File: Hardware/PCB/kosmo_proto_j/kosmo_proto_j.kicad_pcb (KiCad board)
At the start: 2 copper layers, 100 x 55 mm, 567 parts, among them J1 Synth_power_2x5, J10 1x1, J100 1x1, J101 1x1, J102 1x1, J103 1x1, J104 1x1, J105 1x1, J106 1x1, J107 1x1, J108 1x1, J109 1x1, J11 1x1, J110 1x1, J111 1x1, J112 1x1, J113 1x1, J114 1x1, J115 1x1, J116 1x1, J117 1x1, J118 1x1, J119 1x1, J12 1x1, J120 1x1, J121 1x1, J122 1x1, J123 1x1, J124 1x1, J125 1x1, J126 1x1, J127 1x1, J128 1x1, J129 1x1, J13 1x1, J130 1x1, J131 1x1, J132 1x1, J133 1x1, J134 1x1, J135 1x1, J136 1x1, J137 1x1, J138 1x1, J139 1x1, J14 1x1, J140 1x1, J141 1x1, J142 1x1, J143 1x1, J144 1x1, J145 1x1, J146 1x1, J147 1x1, J148 1x1, J149 1x1, J15 1x1, J150 1x1, J151 1x1, J152 1x1, J153 1x1, J154 1x1, J155 1x1, J156 1x1, J157 1x1, J158 1x1, J159 1x1, J16 1x1, J160 1x1, J161 1x1, J162 1x1, J163 1x1, J164 1x1, J165 1x1, J166 1x1, J167 1x1, J168 1x1, J169 1x1, J17 1x1, J170 1x1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

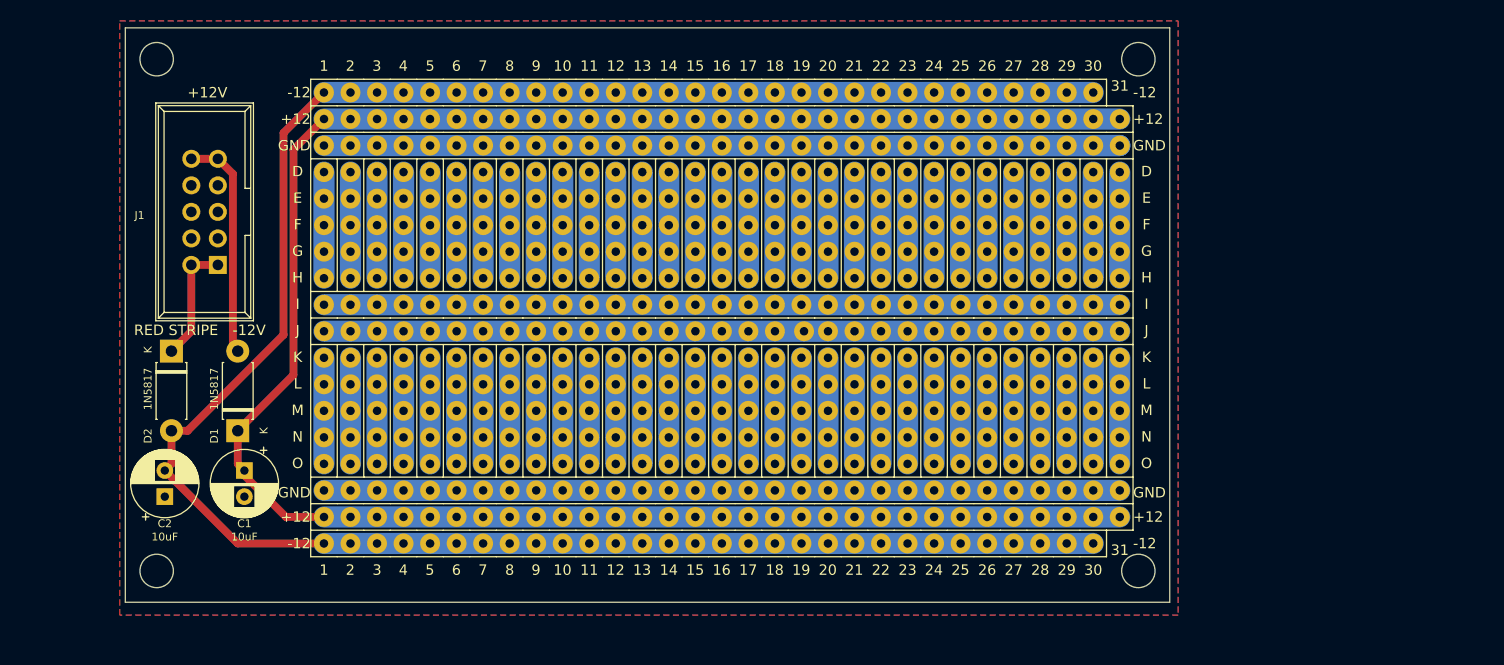
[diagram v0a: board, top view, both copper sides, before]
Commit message: Narrower version with jacks (kosmo_proto_j)
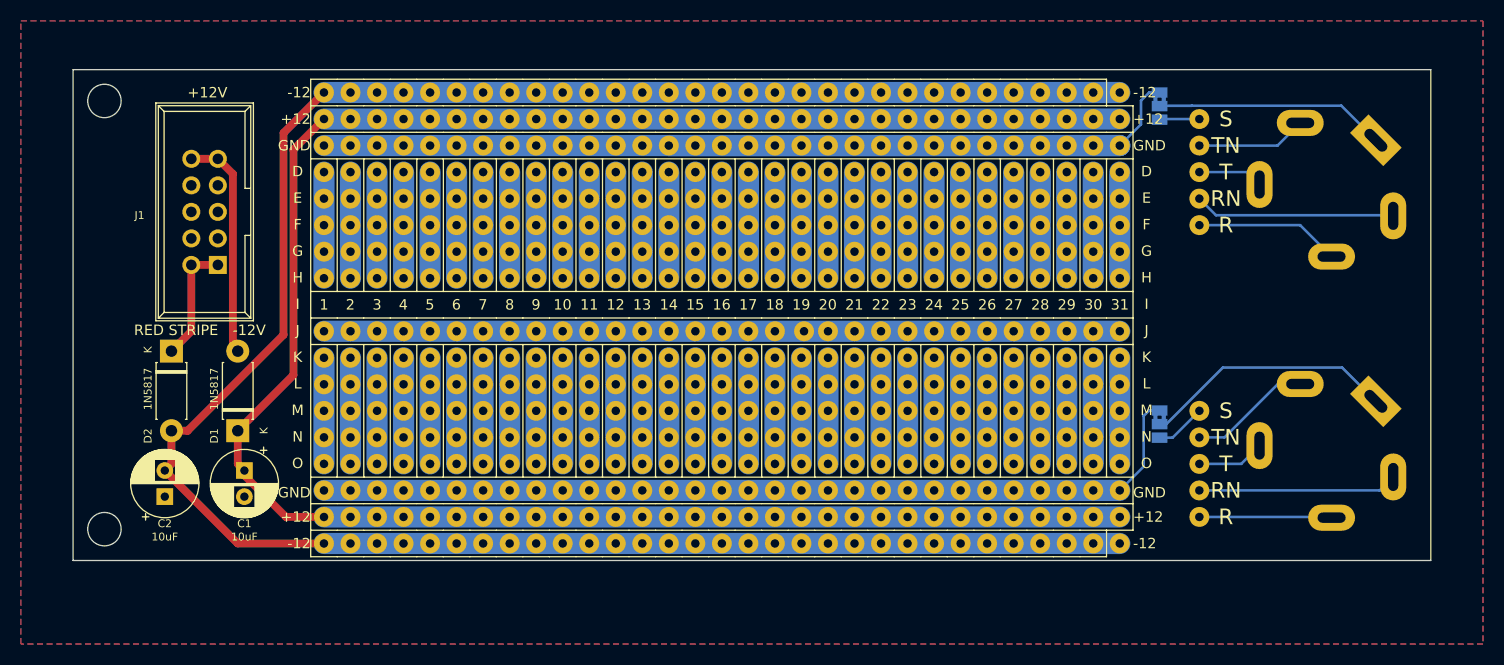
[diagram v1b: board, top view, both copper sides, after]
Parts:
- removed the H2 at (142.8, 105.5)
- removed H4: MountingHole, ao_tht:MountingHole_3.2mm_M3
- removed the J10 at (64.8, 80.0)
- removed the J100 at (90.2, 80.0)
- removed the J109 at (92.7, 80.0)
- removed the J118 at (95.2, 80.0)
- removed the J127 at (97.8, 80.0)
- removed the J136 at (100.3, 80.0)
- removed the J145 at (102.9, 80.0)
- removed the J154 at (105.4, 80.0)
- removed the J163 at (108.0, 80.0)
- removed the J172 at (110.5, 80.0)
- removed the J181 at (113.0, 80.0)
- removed the J19 at (67.3, 80.0)
- removed the J190 at (115.6, 80.0)
- removed the J199 at (118.1, 80.0)
- removed the J208 at (120.7, 80.0)
- removed the J217 at (123.2, 80.0)
- removed the J226 at (125.7, 80.0)
- removed the J235 at (128.3, 80.0)
- removed the J262 at (135.9, 80.0)
- removed the J271 at (138.4, 80.0)
- removed the J28 at (69.8, 80.0)
- removed the J280 at (141.0, 80.0)
- removed the J37 at (72.4, 80.0)
- removed the J46 at (74.9, 80.0)
- removed the J55 at (77.5, 80.0)
- removed the J64 at (80.0, 80.0)
- removed the J73 at (82.5, 80.0)
- removed the J82 at (85.1, 80.0)
- removed the J91 at (87.6, 80.0)
- added J2: AudioJack3_SwitchTR, ao_tht:Jack_6.35mm_PJ_629HAN_slots, B.Cu at (160.8, 69.0)
- added J252: 1x1, ao_tht:Perf_Board_Hole, F.Cu at (148.6, 72.4)
- added J254: 1x1, ao_tht:Perf_Board_Hole, F.Cu at (148.6, 100.3)
- added J255: 1x1, ao_tht:Perf_Board_Hole, F.Cu at (148.6, 95.2)
- added J256: 1x1, ao_tht:Perf_Board_Hole, F.Cu at (148.6, 69.8)
- added J257: 1x1, ao_tht:Perf_Board_Hole, F.Cu at (148.6, 64.8)
- added J258: 1x1, ao_tht:Perf_Board_Hole, F.Cu at (148.6, 97.8)
- added J259: 1x1, ao_tht:Perf_Board_Hole, F.Cu at (148.6, 92.7)
- added J260: 1x1, ao_tht:Perf_Board_Hole, F.Cu at (148.6, 62.2)
- added J261: 1x1, ao_tht:Perf_Board_Hole, F.Cu at (148.6, 90.2)
- added J3: AudioJack3_SwitchTR, ao_tht:Jack_6.35mm_PJ_629HAN_slots, B.Cu at (160.8, 94.0)
- added J540: 1x1, ao_tht:Perf_Board_Hole, F.Cu at (141.0, 102.9)
- added JP1: SolderJumper_3_Bridged12, Jumper:SolderJumper-3_P1.3mm_Bridged2Bar12_Pad1.0x1.5mm, B.Cu at (144.8, 61.0)
- added JP2: SolderJumper_3_Bridged12, Jumper:SolderJumper-3_P1.3mm_Bridged2Bar12_Pad1.0x1.5mm, B.Cu at (144.8, 91.4)
- moved GRAF1 94.1 mm to (148.6, 82.0), turned to 270 degrees
- moved GRAF2 31.1 mm to (60.3, 91.1), turned to 270 degrees
- moved J244 22.7 mm to (141.0, 59.7)
- moved J253 19.8 mm to (148.6, 67.3)
- moved H1 6.40 mm to (43.8, 101.5)
- moved H2 6.40 mm to (43.8, 60.5)
- renumbered H3 to H2, J8 to J10, J110 to J100, J111 to J101, J112 to J102, J113 to J103, J114 to J104, J115 to J105, J116 to J106, J117 to J107, J119 to J108, J120 to J109, J9 to J11, J121 to J110, J122 to J111, J123 to J112, J124 to J113, J125 to J114, J126 to J115, J128 to J116, J129 to J117, J130 to J118, J131 to J119, J11 to J12, J132 to J120, J133 to J121, J134 to J122, J135 to J123, J137 to J124, J138 to J125, J139 to J126, J140 to J127, J141 to J128, J142 to J129, J12 to J13, J143 to J130, J144 to J131, J146 to J132, J147 to J133, J148 to J134, J149 to J135, J150 to J136, J151 to J137, J152 to J138, J153 to J139, J13 to J14, J155 to J140, J156 to J141, J157 to J142, J158 to J143, J159 to J144, J160 to J145, J161 to J146, J162 to J147, J164 to J148, J165 to J149, J14 to J15, J166 to J150, J167 to J151, J168 to J152, J169 to J153, J170 to J154, J171 to J155, J173 to J156, J174 to J157, J175 to J158, J176 to J159, J15 to J16, J177 to J160, J178 to J161, J179 to J162, J180 to J163, J182 to J164, J183 to J165, J184 to J166, J185 to J167, J186 to J168, J187 to J169, J16 to J17, J188 to J170, J189 to J171, J191 to J172, J192 to J173, J193 to J174, J194 to J175, J195 to J176, J196 to J177, J197 to J178, J198 to J179, J17 to J18, J200 to J180, J201 to J181, J202 to J182, J203 to J183, J204 to J184, J205 to J185, J206 to J186, J207 to J187, J209 to J188, J210 to J189, J18 to J19, J211 to J190, J212 to J191, J213 to J192, J214 to J193, J215 to J194, J216 to J195, J218 to J196, J219 to J197, J220 to J198, J221 to J199, J222 to J200, J223 to J201, J224 to J202, J225 to J203, J227 to J204, J228 to J205, J229 to J206, J230 to J207, J231 to J208, J232 to J209, J233 to J210, J234 to J211, J236 to J212, J237 to J213, J238 to J214, J239 to J215, J240 to J216, J241 to J217, J242 to J218, J243 to J219, J245 to J220, J246 to J221, J247 to J222, J248 to J223, J249 to J224, J250 to J225, J251 to J226, J252 to J227, J254 to J228, J255 to J229, J256 to J230, J257 to J231, J258 to J232, J259 to J233, J260 to J234, J261 to J235, J263 to J236, J264 to J237, J265 to J238, J266 to J239, J267 to J240, J268 to J241, J269 to J242, J270 to J243, J273 to J245, J274 to J246, J275 to J247, J276 to J248, J277 to J249, J278 to J250, J279 to J251, J281 to J262, J282 to J263, J283 to J264, J284 to J265, J285 to J266, J286 to J267, J287 to J268, J288 to J269, J289 to J270, J290 to J271, J291 to J272, J292 to J273, J293 to J274, J294 to J275, J295 to J276, J296 to J277, J297 to J278, J298 to J279, J29 to J28, J299 to J280, J300 to J281, J301 to J282, J302 to J283, J303 to J284, J304 to J285, J305 to J286, J306 to J287, J307 to J288, J308 to J289, J30 to J29, J309 to J290, J310 to J291, J311 to J292, J312 to J293, J313 to J294, J314 to J295, J315 to J296, J316 to J297, J317 to J298, J318 to J299, J31 to J30, J319 to J300, J320 to J301, J321 to J302, J322 to J303, J323 to J304, J324 to J305, J325 to J306, J326 to J307, J327 to J308, J328 to J309, J32 to J31, J329 to J310, J330 to J311, J331 to J312, J332 to J313, J333 to J314, J334 to J315, J335 to J316, J336 to J317, J337 to J318, J338 to J319, J33 to J32, J339 to J320, J340 to J321, J341 to J322, J342 to J323, J343 to J324, J344 to J325, J345 to J326, J346 to J327, J347 to J328, J348 to J329, J34 to J33, J349 to J330, J350 to J331, J351 to J332, J352 to J333, J353 to J334, J354 to J335, J355 to J336, J356 to J337, J357 to J338, J358 to J339, J35 to J34, J359 to J340, J360 to J341, J361 to J342, J362 to J343, J363 to J344, J364 to J345, J365 to J346, J366 to J347, J367 to J348, J368 to J349, J36 to J35, J369 to J350, J370 to J351, J371 to J352, J372 to J353, J373 to J354, J374 to J355, J375 to J356, J376 to J357, J377 to J358, J378 to J359, J38 to J36, J379 to J360, J380 to J361, J381 to J362, J382 to J363, J383 to J364, J384 to J365, J385 to J366, J386 to J367, J387 to J368, J388 to J369, J39 to J37, J389 to J370, J390 to J371, J391 to J372, J392 to J373, J393 to J374, J394 to J375, J395 to J376, J396 to J377, J397 to J378, J398 to J379, J40 to J38, J399 to J380, J400 to J381, J401 to J382, J402 to J383, J403 to J384, J404 to J385, J405 to J386, J406 to J387, J407 to J388, J408 to J389, J41 to J39, J409 to J390, J410 to J391, J411 to J392, J412 to J393, J413 to J394, J414 to J395, J415 to J396, J416 to J397, J417 to J398, J418 to J399, J2 to J4, J42 to J40, J419 to J400, J420 to J401, J421 to J402, J422 to J403, J423 to J404, J424 to J405, J425 to J406, J426 to J407, J427 to J408, J428 to J409, J43 to J41, J429 to J410, J430 to J411, J431 to J412, J432 to J413, J433 to J414, J434 to J415, J435 to J416, J436 to J417, J437 to J418, J438 to J419, J44 to J42, J439 to J420, J440 to J421, J441 to J422, J442 to J423, J443 to J424, J444 to J425, J445 to J426, J446 to J427, J447 to J428, J448 to J429, J45 to J43, J449 to J430, J450 to J431, J451 to J432, J452 to J433, J453 to J434, J454 to J435, J455 to J436, J456 to J437, J457 to J438, J458 to J439, J47 to J44, J459 to J440, J460 to J441, J461 to J442, J462 to J443, J463 to J444, J464 to J445, J465 to J446, J466 to J447, J467 to J448, J468 to J449, J48 to J45, J469 to J450, J470 to J451, J471 to J452, J472 to J453, J473 to J454, J474 to J455, J475 to J456, J476 to J457, J477 to J458, J478 to J459, J49 to J46, J479 to J460, J480 to J461, J481 to J462, J482 to J463, J483 to J464, J484 to J465, J485 to J466, J486 to J467, J487 to J468, J488 to J469, J50 to J47, J489 to J470, J490 to J471, J491 to J472, J492 to J473, J493 to J474, J494 to J475, J495 to J476, J496 to J477, J497 to J478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
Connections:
- J244 pad 1: Net-(J10-Pad1) (its old number) -> -12V
- J253 pad 1: Net-(J10-Pad1) (its old number) -> Net-(J2-PadT)
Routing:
- net Net-(J10-Pad1) (its old number): track 76.2 -> 0.00 mm
- net Net-(J3-PadS): track 0.00 -> 24.3 mm
- net Net-(J2-PadS): track 0.00 -> 22.1 mm
- net Net-(J2-PadRN): track 0.00 -> 19.2 mm
- net Net-(J258-Pad1): track 0.00 -> 19.1 mm
- net GND: track 195.6 -> 212.6 mm
- net Net-(J2-PadR): track 0.00 -> 13.9 mm
- net Net-(J254-Pad1): track 0.00 -> 12.7 mm
- net Net-(J259-Pad1): track 0.00 -> 11.8 mm
- net Net-(J2-PadTN): track 0.00 -> 10.6 mm
- net Net-(J255-Pad1): track 0.00 -> 6.48 mm
- net Net-(J2-PadT): track 0.00 -> 6.25 mm
- net -12V: track 208.9 -> 214.0 mm
- net Net-(J261-Pad1): track 0.00 -> 4.87 mm
- net Net-(J260-Pad1): track 0.00 -> 3.81 mm
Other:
- board size 100 x 55 mm -> 130 x 47 mm
- board text added: "R"
- board text added: "RN"
- board text added: "S"
- board text added: "T"
- board text added: "TN"

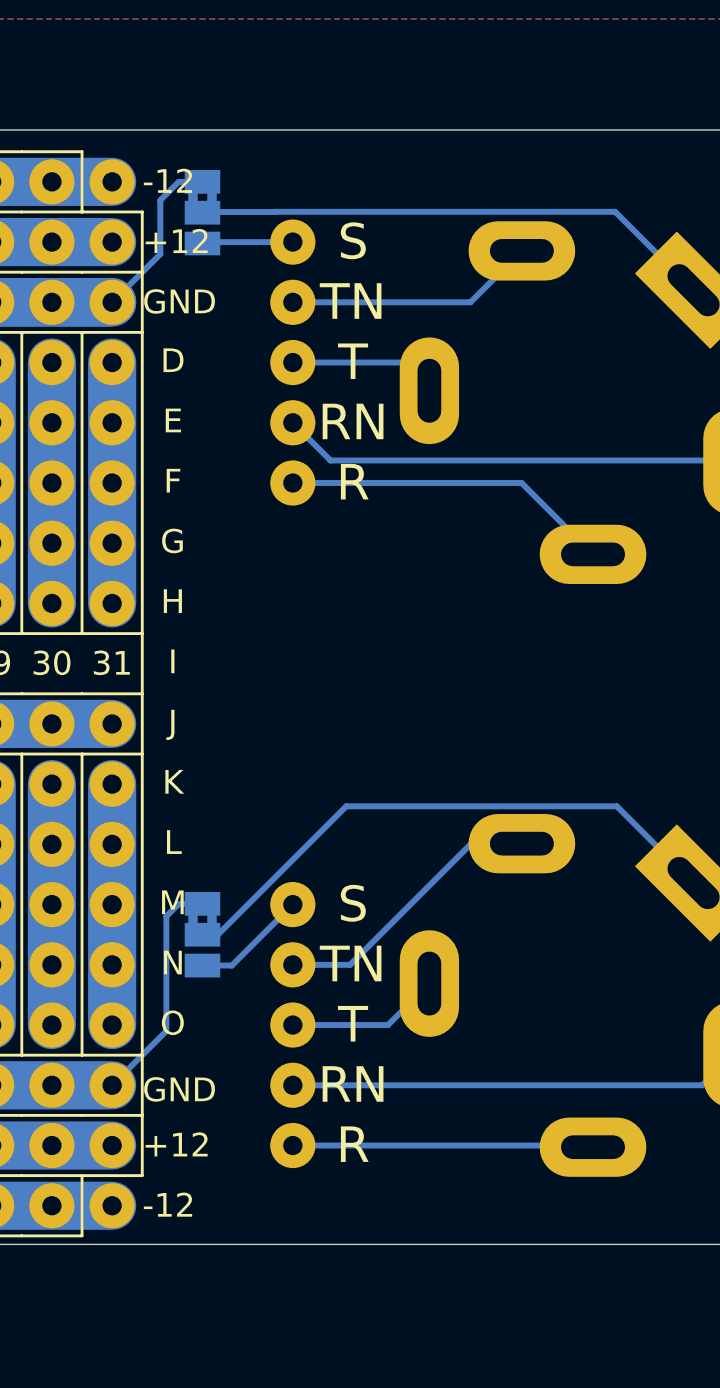
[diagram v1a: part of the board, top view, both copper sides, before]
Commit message: Jack labels; images
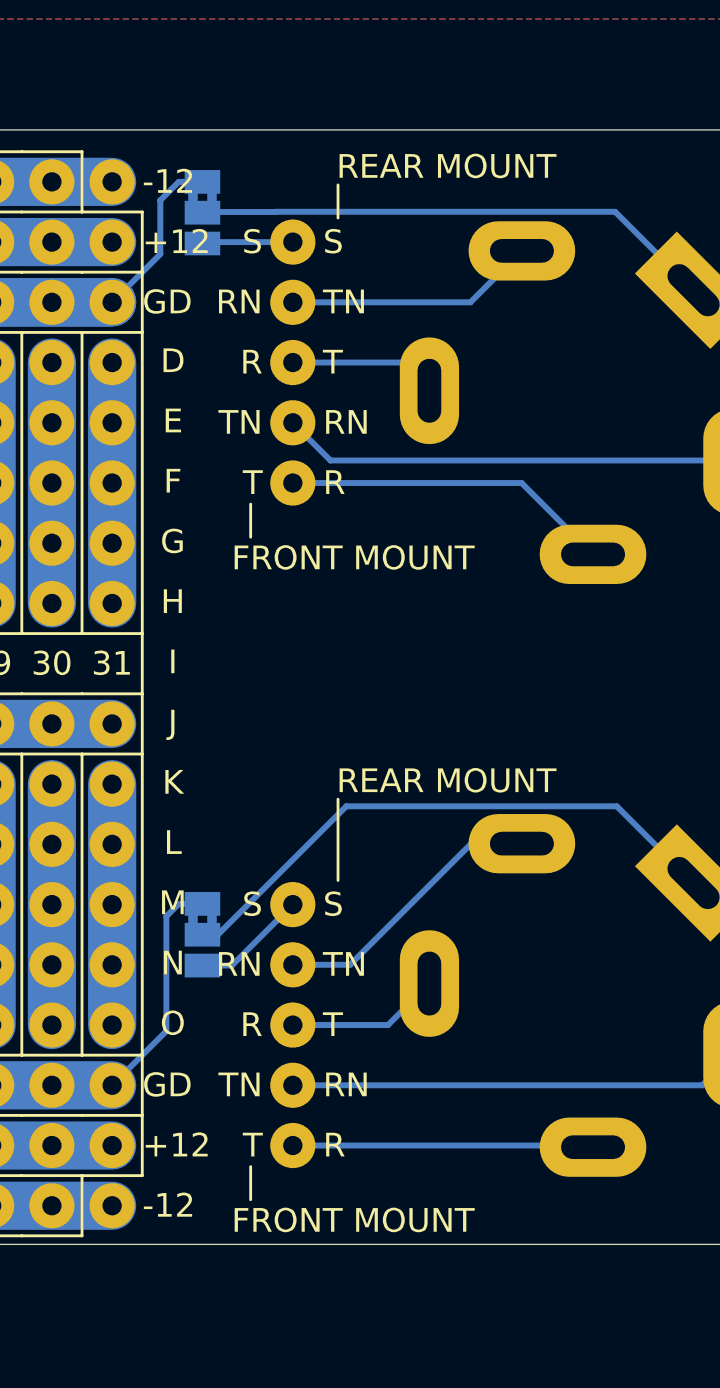
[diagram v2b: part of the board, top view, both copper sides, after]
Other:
- board text added: "FRONT MOUNT"
- board text added: "GD"
- board text added: "REAR MOUNT"

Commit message: more jacks mod, tweak original
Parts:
- D1, D2: footprint ao_tht:D_DO-41_SOD81_P7.62mm_Horizontal -> ao_tht:D_DO-41_SOD81_P10.16mm_Horizontal
- moved J1 2.54 mm to (54.6, 73.7)
- moved D2 2.01 mm to (49.5, 82.5)
- moved J2 2.00 mm to (162.8, 69.0)
- moved J252 2.00 mm to (150.6, 72.4)
- moved J253 2.00 mm to (150.6, 67.3)
- moved J254 2.00 mm to (150.6, 100.3)
- moved J255 2.00 mm to (150.6, 95.2)
- moved J256 2.00 mm to (150.6, 69.8)
- moved J257 2.00 mm to (150.6, 64.8)
- moved J258 2.00 mm to (150.6, 97.8)
- moved J259 2.00 mm to (150.6, 92.7)
- moved J260 2.00 mm to (150.6, 62.2)
- moved J261 2.00 mm to (150.6, 90.2)
- moved J3 2.00 mm to (162.8, 94.0)
- moved JP1 2.00 mm to (146.8, 61.0)
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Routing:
- net GND: track 212.6 -> 216.6 mm
- net Net-(J2-PadTN): track 10.6 -> 8.56 mm
- net Net-(D2-Pad1): track 11.6 -> 12.5 mm
- net Net-(D1-Pad2): track 21.7 -> 22.6 mm
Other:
- board size 130 x 47 mm -> 132 x 47 mm
- board text removed: "GD"
